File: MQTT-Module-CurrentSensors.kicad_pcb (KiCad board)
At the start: 4 copper layers, 44 x 58.4 mm, 68 parts, among them IC401 16 Bit ADC, J301 A2541WV-10P, J302 A2541WV-10P, J303 A2541WV-2x3P, J304 1715747, U201 ATmega328PB-A, U501 Precision ZD RR, U502 Precision ZD RR, U503 Precision ZD RR

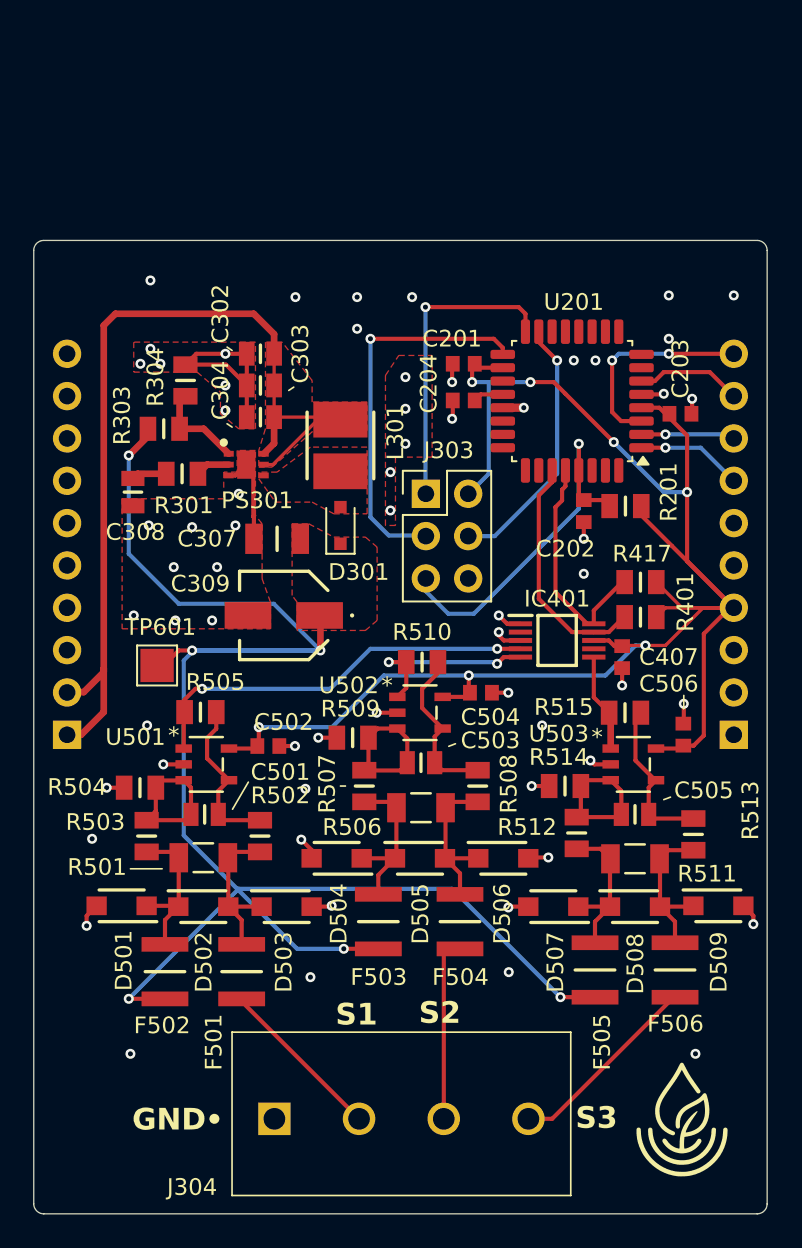
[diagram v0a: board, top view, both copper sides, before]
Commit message: Removed one PTC per sensor as it shouldn't be required. Adjusted routing to star pattern.
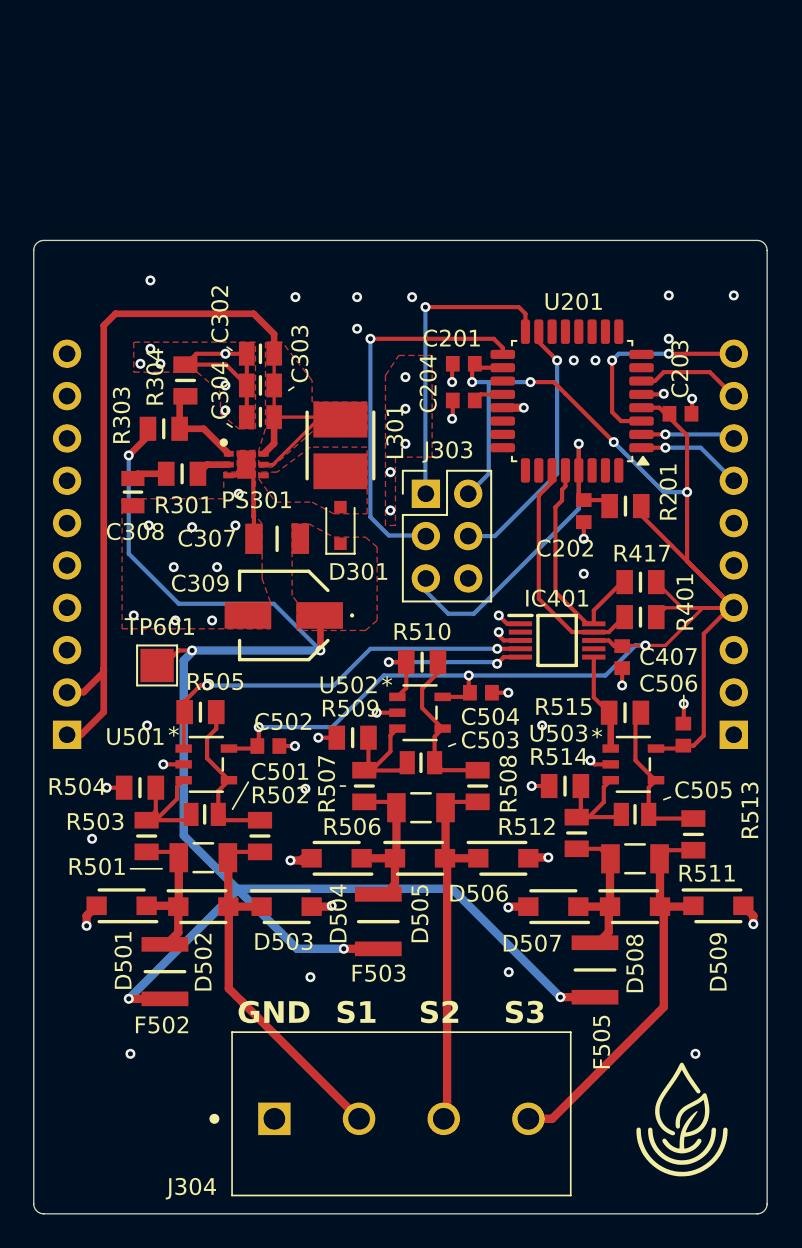
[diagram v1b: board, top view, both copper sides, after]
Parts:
- removed F501, F504, F506: 50mA 30V, PTC, BOURNS Fuses:FUSC3226X110N
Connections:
- D502 pad 2: Net-(D502-A2) -> /SensorRecievers/Sensor1
- D503 pad 1: Net-(D502-A2) -> /SensorRecievers/Sensor1
- D505 pad 2: Net-(D505-A2) -> /SensorRecievers/Sensor2
- D506 pad 1: Net-(D505-A2) -> /SensorRecievers/Sensor2
- D508 pad 2: Net-(D508-A2) -> /SensorRecievers/Sensor3
- D509 pad 1: Net-(D508-A2) -> /SensorRecievers/Sensor3
- R501 pad 1: Net-(D502-A2) -> /SensorRecievers/Sensor1
- R502 pad 1: Net-(D502-A2) -> /SensorRecievers/Sensor1
- R506 pad 1: Net-(D505-A2) -> /SensorRecievers/Sensor2
- R508 pad 1: Net-(D505-A2) -> /SensorRecievers/Sensor2
- R511 pad 1: Net-(D508-A2) -> /SensorRecievers/Sensor3
- R513 pad 1: Net-(D508-A2) -> /SensorRecievers/Sensor3
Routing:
- net /SensorRecievers/Sensor1: track 10.1 -> 23.0 mm
- net /SensorRecievers/Sensor3: track 11.8 -> 24.2 mm
- net /SensorRecievers/Sensor2: track 11.2 -> 22.9 mm
- net Net-(D508-A2): track 9.75 -> 0.00 mm
- net Net-(D505-A2): track 9.70 -> 0.00 mm
- net Net-(D502-A2): track 9.61 -> 0.00 mm
- net +25V: track 103.4 -> 95.8 mm
- net Net-(U503-+): track 9.20 -> 8.44 mm
- net Net-(U502-+): track 9.12 -> 8.44 mm

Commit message: Updated trace widths and routing. Improved SDA/SCL lines.
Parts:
- moved R401 7.80 mm to (147.2, 100.0), turned to -90 degrees
- moved R417 2.94 mm to (151.6, 100.0), turned to -90 degrees
- moved C202 0.20 mm to (151.2, 96.6)
- moved R201 0.20 mm to (153.7, 96.3)
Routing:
- net +3V3: track 112.3 -> 117.3 mm, vias 7 -> 9
- net /Controller/SDA0: track 6.36 -> 9.65 mm, vias 0 -> 1
- net /AnalogDigitalConverter/SCL1: track 14.0 -> 12.1 mm
- net /Controller/SCL0: track 12.6 -> 14.2 mm, vias 2 -> 1
- net /AnalogDigitalConverter/SDA1: track 14.4 -> 13.5 mm
- net GND: track 46.8 -> 47.3 mm, vias 63 -> 65

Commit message: Updated the diodes to fix issue. Now running 28V diodes for protection of sensing circuit.
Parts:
- removed D501, D502, D503, D504, D505, D506, D507, D508, D509: 13.3V 0.1uA Leak, LITTELFUSE Diodes:SODFL3619X98N
- added D401: 28V 1uA Leak, LITTELFUSE Diodes:SODFL3619X98N, F.Cu at (123.0, 120.3)
- added D402: 28V 1uA Leak, LITTELFUSE Diodes:SODFL3619X98N, F.Cu at (128.2, 120.3)
- added D403: 28V 1uA Leak, LITTELFUSE Diodes:SODFL3619X98N, F.Cu at (133.4, 120.3)
- added D404: 28V 1uA Leak, LITTELFUSE Diodes:SODFL3619X98N, F.Cu at (136.1, 117.4)
- added D405: 28V 1uA Leak, LITTELFUSE Diodes:SODFL3619X98N, F.Cu at (141.3, 117.5)
- added D406: 28V 1uA Leak, LITTELFUSE Diodes:SODFL3619X98N, F.Cu at (146.4, 117.5)
- added D407: 28V 1uA Leak, LITTELFUSE Diodes:SODFL3619X98N, F.Cu at (148.9, 120.3)
- added D408: 28V 1uA Leak, LITTELFUSE Diodes:SODFL3619X98N, F.Cu at (154.1, 120.3)
- added D409: 28V 1uA Leak, LITTELFUSE Diodes:SODFL3619X98N, F.Cu at (159.3, 120.4)
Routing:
- net GND: track 47.3 -> 47.9 mm

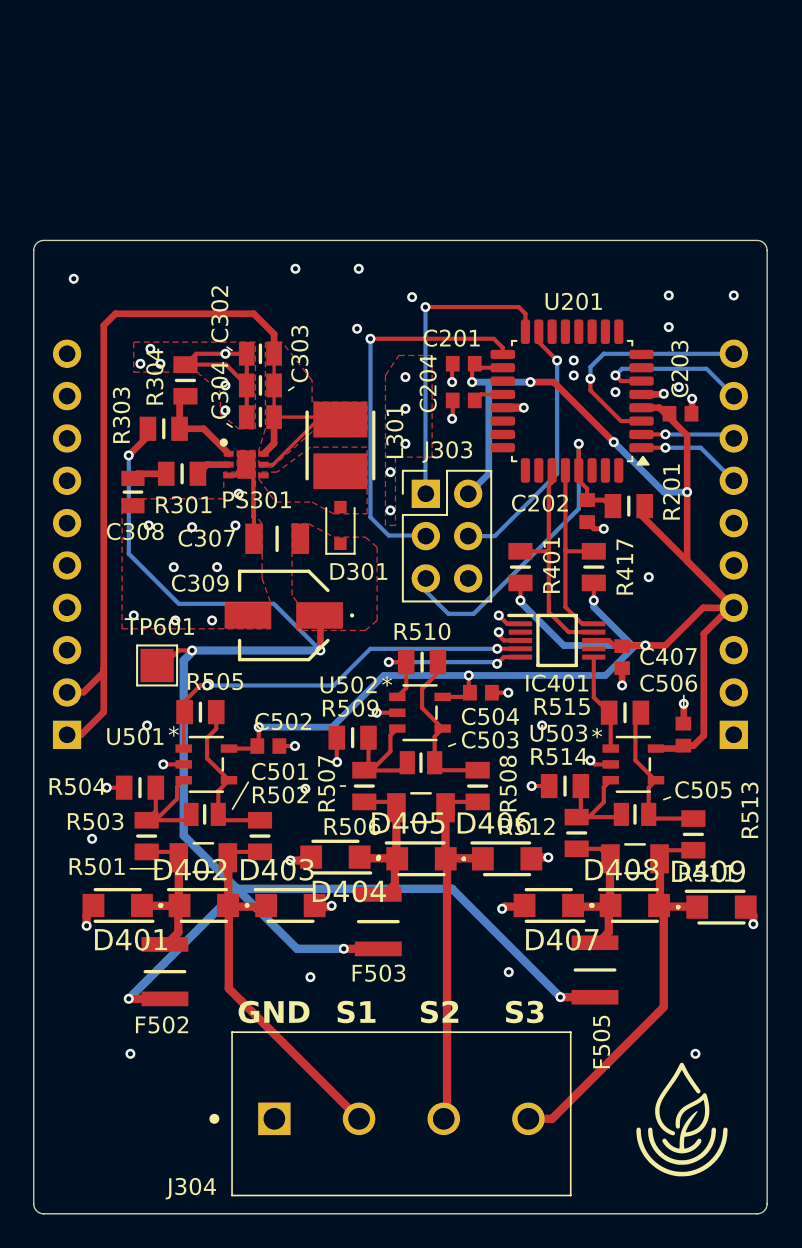
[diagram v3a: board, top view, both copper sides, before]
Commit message: Redid the layout to shrink the board. Updated the silkscreen and updated the footprints to better reflect polarities and support a fab pdf.
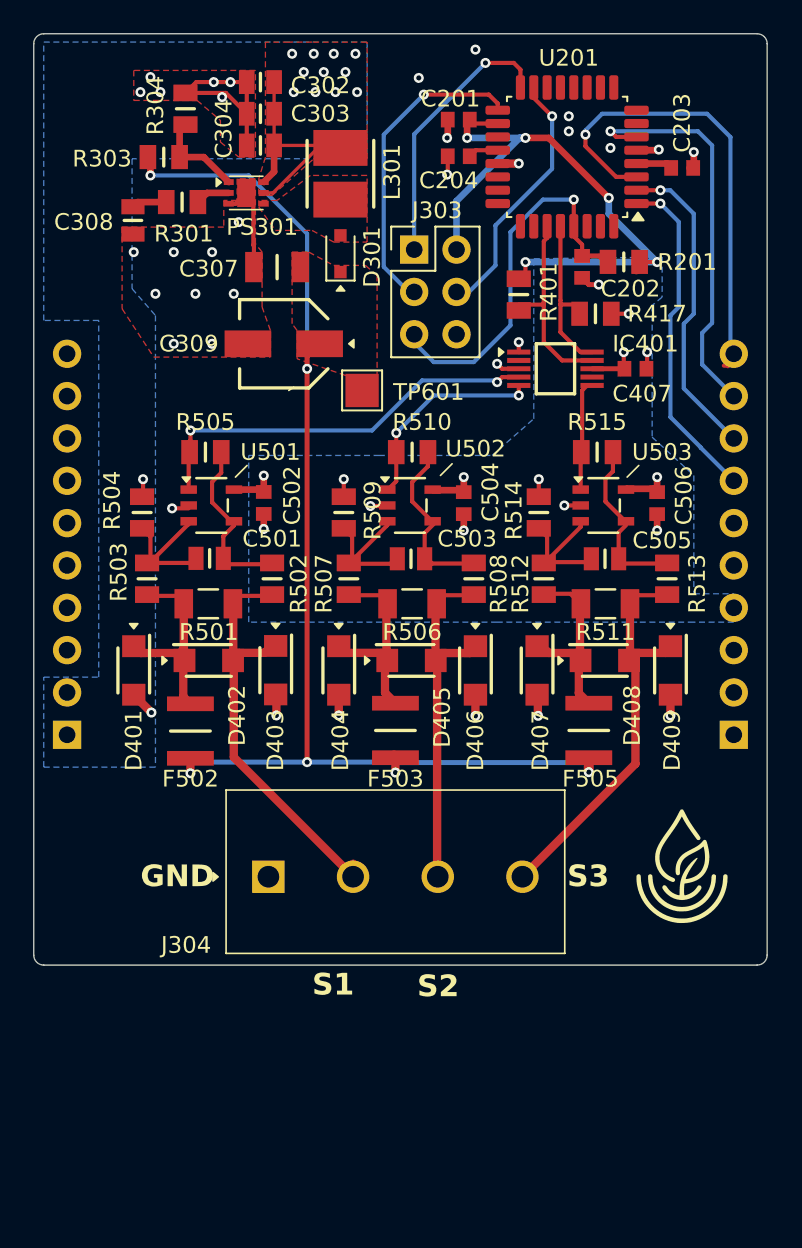
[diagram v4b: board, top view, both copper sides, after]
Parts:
- moved TP601 20.6 mm to (137.7, 89.4)
- moved C407 17.3 mm to (154.1, 88.1), turned to 180 degrees
- moved R504 16.5 mm to (124.5, 96.7), turned to 90 degrees
- moved R514 16.5 mm to (148.3, 96.7), turned to 90 degrees
- moved R401 16.4 mm to (147.1, 83.7), turned to 90 degrees
- moved IC401 16.3 mm to (149.3, 88.1)
- moved C309 16.3 mm to (133.0, 86.6)
- moved R301 16.3 mm to (126.9, 78.1)
- moved C302 16.3 mm to (131.6, 70.9)
- moved C303 16.3 mm to (131.6, 72.8)
- moved C304 16.3 mm to (131.6, 74.7)
- moved C307 16.3 mm to (132.6, 82.0)
- moved C308 16.3 mm to (124.0, 79.2)
- moved D301 16.3 mm to (136.4, 81.2)
- moved L301 16.3 mm to (136.4, 76.4)
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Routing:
- net +3V3: track 117.3 -> 53.9 mm, vias 9 -> 10
- net +12V: track 57.3 -> 16.3 mm, vias 0 -> 11
- net +25V: track 95.8 -> 72.4 mm
- net /Controller/SDA0: track 9.65 -> 24.2 mm
- net /Controller/MOD: track 6.36 -> 20.3 mm
- net /Controller/SCL0: track 14.2 -> 27.9 mm
- net /Controller/SNS: track 5.64 -> 19.0 mm
- net /Controller/SCK: track 23.4 -> 19.1 mm
- net Net-(D401-A1): track 9.63 -> 13.2 mm
- net /SensorRecievers/Sensor1: track 23.0 -> 26.0 mm
- net Net-(D404-A1): track 10.3 -> 12.8 mm
- net GND: track 47.9 -> 45.6 mm, vias 65 -> 44
- net /Controller/MISO: track 18.5 -> 16.3 mm
- net Net-(D407-A1): track 9.85 -> 11.8 mm
- net /AnalogDigitalConverter/SCL1: track 12.1 -> 10.4 mm
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- added copper zone on B.Cu, net +12V
- added copper zone on B.Cu, net +3V3
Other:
- board size 44 x 58.4 mm -> 44 x 55.9 mm
